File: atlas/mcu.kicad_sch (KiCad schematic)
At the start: 44 parts, among them J301 Micro_SD_Card, J302 FTSH-105-01-F-DV-007-K, J303 USB_B, J304 TC2030, J305 UB-20PMFP-LC7002, SW301 SW_Push, U301 REF3033, U302 STM32H743BITx, U303 USBLC6-2SC6, Y301 16MHz, Y302 32khz

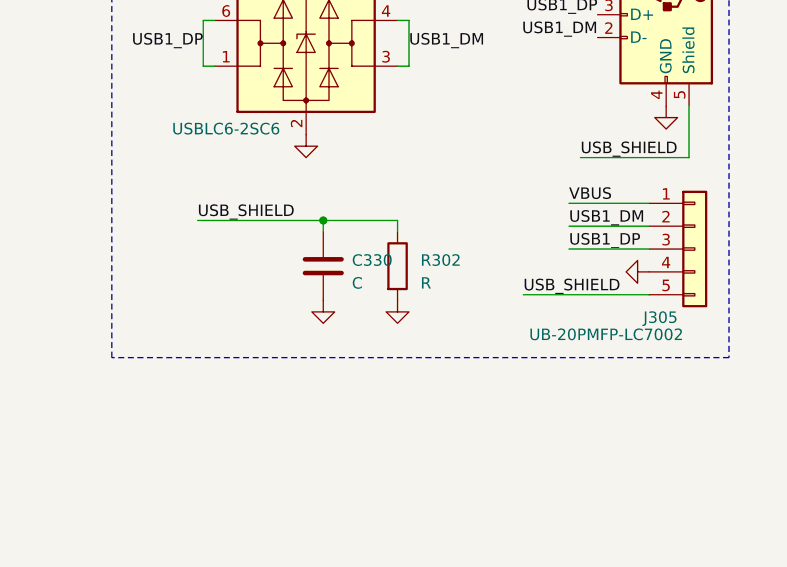
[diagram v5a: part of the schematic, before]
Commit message: footprints & lcsc
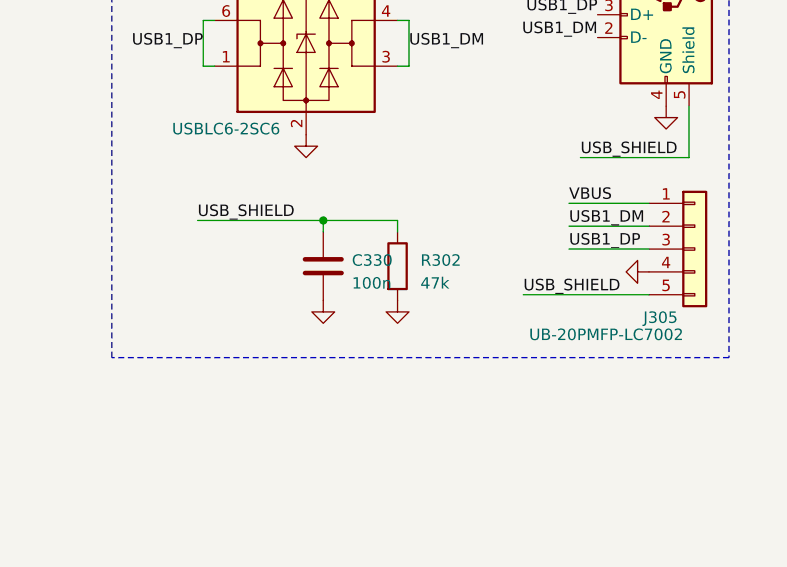
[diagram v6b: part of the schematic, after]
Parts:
- C327, C328: footprint (none) -> Capacitor_SMD:C_0402_1005Metric
- C330: value C -> 100n; footprint (none) -> Capacitor_SMD:C_0603_1608Metric; LCSC (none) -> C14663
- FB301: footprint (none) -> Inductor_SMD:L_0805_2012Metric; LCSC (none) -> C1015
- J303: LCSC (none) -> C456341
- R301: footprint (none) -> Resistor_SMD:R_0402_1005Metric; LCSC (none) -> C25744
- R302: value R -> 47k; footprint (none) -> Resistor_SMD:R_0603_1608Metric; LCSC (none) -> C25819
- U301: LCSC C130016 -> C36658
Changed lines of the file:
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@@
       (effects (font (size 1.27 1.27)) (justify left))
     )
-    (property "Footprint" "" (id 2) (at 31.877 88.265 90)
+    (property "Footprint" "Resistor_SMD:R_0402_1005Metric" (id 2) (at 31.877 88.265 90)
       (effects (font (size 1.27 1.27)) hide)
     )
@@
       (effects (font (size 1.27 1.27)) hide)
     )
+    (property "LCSC" "C25744" (id 4) (at 33.655 88.265 0)
+      (effects (font (size 1.27 1.27)) hide)
+    )
     (pin "1")
     (pin "2")
@@
       (effects (font (size 1.27 1.27)) (justify left))
     )
-    (property "Value" "R" (id 1) (at 225.425 194.9449 0)
-      (effects (font (size 1.27 1.27)) (justify left))
-    )
-    (property "Footprint" "" (id 2) (at 221.107 193.04 90)
+    (property "Value" "47k" (id 1) (at 225.425 194.9449 0)
+      (effects (font (size 1.27 1.27)) (justify left))
+    )
+    (property "Footprint" "Resistor_SMD:R_0603_1608Metric" (id 2) (at 221.107 193.04 90)
       (effects (font (size 1.27 1.27)) hide)
     )
     (property "Datasheet" "~" (id 3) (at 222.885 193.04 0)
+      (effects (font (size 1.27 1.27)) hide)
+    )
+    (property "LCSC" "C25819" (id 4) (at 222.885 193.04 0)
       (effects (font (size 1.27 1.27)) hide)
     )
@@
       (effects (font (size 1.27 1.27)) (justify left))
     )
-    (property "Footprint" "" (id 2) (at 43.5102 104.775 0)
+    (property "Footprint" "Capacitor_SMD:C_0402_1005Metric" (id 2) (at 43.5102 104.775 0)
       (effects (font (size 1.27 1.27)) hide)
     )
@@
       (effects (font (size 1.27 1.27)) (justify left))
     )
-    (property "Footprint" "" (id 2) (at 115.9002 126.365 0)
+    (property "Footprint" "Capacitor_SMD:C_0402_1005Metric" (id 2) (at 115.9002 126.365 0)
       (effects (font (size 1.27 1.27)) hide)
     )
@@
       (effects (font (size 1.27 1.27)) (justify left))
     )
-    (property "Value" "C" (id 1) (at 217.805 194.9449 0)
-      (effects (font (size 1.27 1.27)) (justify left))
-    )
-    (property "Footprint" "" (id 2) (at 215.5952 196.85 0)
+    (property "Value" "100n" (id 1) (at 217.805 194.9449 0)
+      (effects (font (size 1.27 1.27)) (justify left))
+    )
+    (property "Footprint" "Capacitor_SMD:C_0603_1608Metric" (id 2) (at 215.5952 196.85 0)
       (effects (font (size 1.27 1.27)) hide)
     )
     (property "Datasheet" "~" (id 3) (at 214.63 193.04 0)
+      (effects (font (size 1.27 1.27)) hide)
+    )
+    (property "LCSC" "C14663" (id 4) (at 214.63 193.04 0)
       (effects (font (size 1.27 1.27)) hide)
     )
@@
       (effects (font (size 1.27 1.27)) hide)
     )
-    (property "Footprint" "" (id 2) (at 132.08 118.618 90)
+    (property "Footprint" "Inductor_SMD:L_0805_2012Metric" (id 2) (at 132.08 118.618 90)
       (effects (font (size 1.27 1.27)) hide)
     )
     (property "Datasheet" "~" (id 3) (at 132.08 116.84 0)
+      (effects (font (size 1.27 1.27)) hide)
+    )
+    (property "LCSC" "C1015" (id 4) (at 132.08 116.84 0)
       (effects (font (size 1.27 1.27)) hide)
     )
@@
       (effects (font (size 1.27 1.27) italic) hide)
     )
-    (property "LCSC" "C130016" (id 4) (at 45.085 52.07 0)
+    (property "LCSC" "C36658" (id 4) (at 45.085 52.07 0)
       (effects (font (size 1.27 1.27)) hide)
     )
@@
       (effects (font (size 1.27 1.27)) hide)
     )
+    (property "LCSC" "C456341" (id 4) (at 252.73 165.1 0)
+      (effects (font (size 1.27 1.27)) hide)
+    )
